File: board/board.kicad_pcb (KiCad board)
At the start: 2 copper layers, 2 parts, among them U1 CC56-12SURKWA

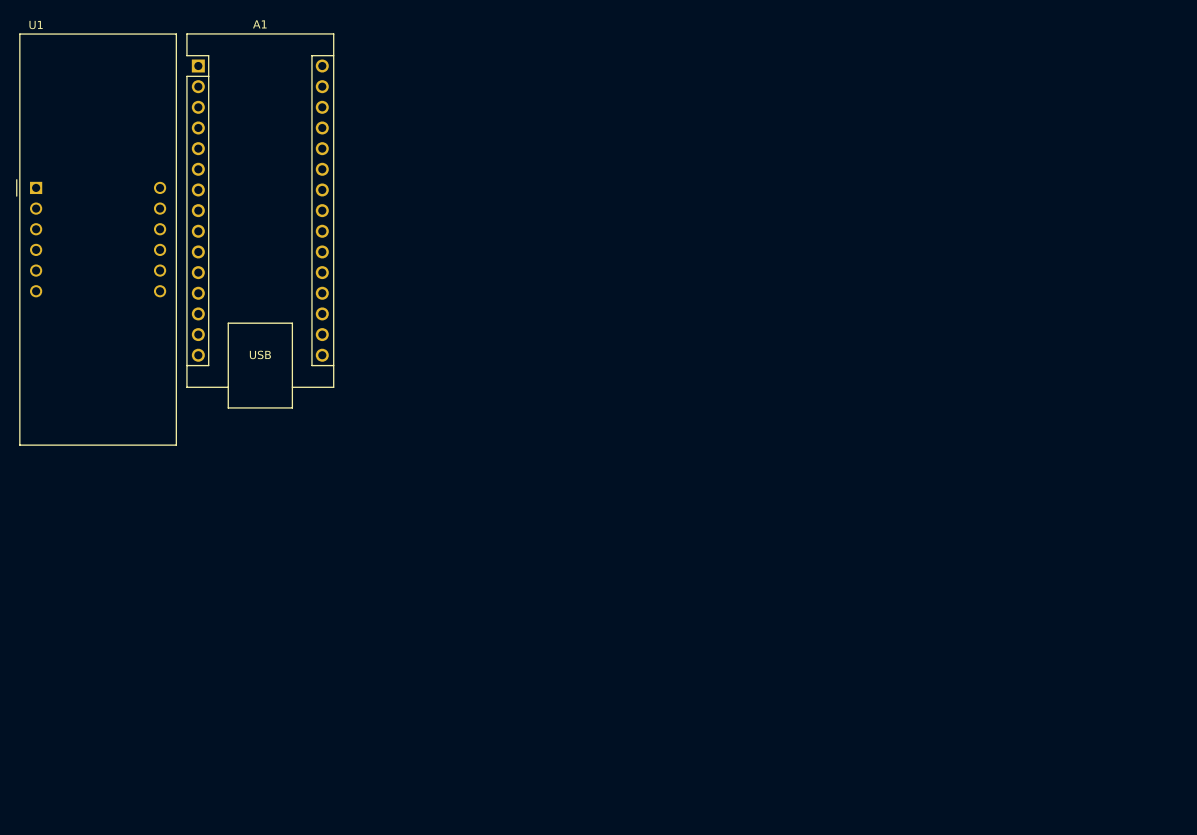
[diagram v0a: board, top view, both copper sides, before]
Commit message: implement part of the wiring
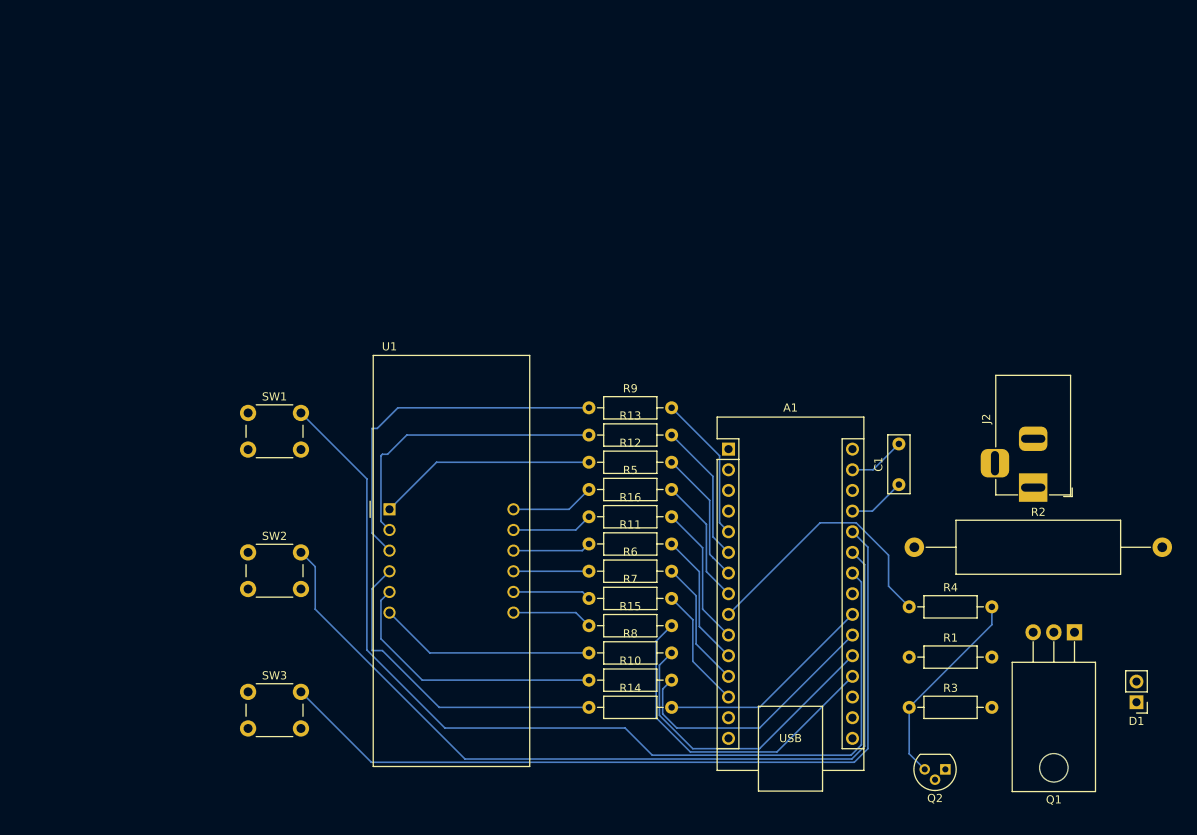
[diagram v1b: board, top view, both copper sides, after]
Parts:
- added C1: 100n, Capacitor_THT:C_Disc_D7.0mm_W2.5mm_P5.00mm, F.Cu at (159.4, 106.0)
- added D1: LED, Connector_PinHeader_2.54mm:PinHeader_1x02_P2.54mm_Vertical, F.Cu at (188.6, 132.7)
- added J2: Barrel_Jack_Switch, Connector_BarrelJack:BarrelJack_Horizontal, F.Cu at (175.9, 106.3)
- added Q1: Q_PMOS_GDS, Package_TO_SOT_THT:TO-220-3_Horizontal_TabDown, F.Cu at (181.0, 124.1)
- added Q2: Q_NPN_ECB, Package_TO_SOT_THT:TO-92, F.Cu at (165.1, 141.0)
- added R1: 10k, Resistor_THT:R_Axial_DIN0207_L6.3mm_D2.5mm_P10.16mm_Horizontal, F.Cu at (160.7, 127.2)
- added R10: 300, Resistor_THT:R_Axial_DIN0207_L6.3mm_D2.5mm_P10.16mm_Horizontal, F.Cu at (121.3, 130.0)
- added R11: 300, Resistor_THT:R_Axial_DIN0207_L6.3mm_D2.5mm_P10.16mm_Horizontal, F.Cu at (121.3, 113.3)
- added R12: 300, Resistor_THT:R_Axial_DIN0207_L6.3mm_D2.5mm_P10.16mm_Horizontal, F.Cu at (121.3, 103.2)
- added R13: 300, Resistor_THT:R_Axial_DIN0207_L6.3mm_D2.5mm_P10.16mm_Horizontal, F.Cu at (121.3, 99.9)
- added R14: 300, Resistor_THT:R_Axial_DIN0207_L6.3mm_D2.5mm_P10.16mm_Horizontal, F.Cu at (121.3, 133.3)
- added R15: 300, Resistor_THT:R_Axial_DIN0207_L6.3mm_D2.5mm_P10.16mm_Horizontal, F.Cu at (121.3, 123.3)
- added R16: 300, Resistor_THT:R_Axial_DIN0207_L6.3mm_D2.5mm_P10.16mm_Horizontal, F.Cu at (121.3, 109.9)
- added R2: 15R, 5W, Resistor_THT:R_Axial_Power_L20.0mm_W6.4mm_P30.48mm, F.Cu at (161.3, 113.7)
- added R3: 10k, Resistor_THT:R_Axial_DIN0207_L6.3mm_D2.5mm_P10.16mm_Horizontal, F.Cu at (160.7, 133.3)
- added R4: 10k, Resistor_THT:R_Axial_DIN0207_L6.3mm_D2.5mm_P10.16mm_Horizontal, F.Cu at (160.7, 121.0)
- added R5: 300, Resistor_THT:R_Axial_DIN0207_L6.3mm_D2.5mm_P10.16mm_Horizontal, F.Cu at (121.3, 106.6)
- added R6: 300, Resistor_THT:R_Axial_DIN0207_L6.3mm_D2.5mm_P10.16mm_Horizontal, F.Cu at (121.3, 116.6)
- added R7: 300, Resistor_THT:R_Axial_DIN0207_L6.3mm_D2.5mm_P10.16mm_Horizontal, F.Cu at (121.3, 120.0)
- added R8: 300, Resistor_THT:R_Axial_DIN0207_L6.3mm_D2.5mm_P10.16mm_Horizontal, F.Cu at (121.3, 126.7)
- added R9: 300, Resistor_THT:R_Axial_DIN0207_L6.3mm_D2.5mm_P10.16mm_Horizontal, F.Cu at (121.3, 96.5)
- added SW1: SW_Push, Button_Switch_THT:SW_PUSH_6mm_H7.3mm, F.Cu at (79.4, 97.2)
- added SW2: SW_Push, Button_Switch_THT:SW_PUSH_6mm_H7.3mm, F.Cu at (79.4, 114.3)
- added SW3: SW_Push, Button_Switch_THT:SW_PUSH_6mm_H7.3mm, F.Cu at (79.4, 131.4)
- moved A1 80.4 mm to (138.4, 101.6)
- moved U1 58.7 mm to (96.8, 109.0)
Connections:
- A1 pad 22: unconnected-(A1-A3-Pad22) -> Net-(A1-A3)
- A1 pad 23: Net-(A1-SDA/A4) -> unconnected-(A1-SDA/A4-Pad23)
- A1 pad 27: unconnected-(A1-+5V-Pad27) -> Net-(A1-+5V)
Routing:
- net Net-(A1-SCL/A5): track 0.00 -> 120.8 mm
- net Net-(A1-A6): track 0.00 -> 108.0 mm
- net Net-(A1-A7): track 0.00 -> 101.4 mm
- net Net-(U1-DPX): track 0.00 -> 43.6 mm
- net Net-(A1-A0): track 0.00 -> 41.8 mm
- net Net-(U1-c): track 0.00 -> 40.2 mm
- net Net-(A1-A1): track 0.00 -> 38.5 mm
- net Net-(U1-d): track 0.00 -> 36.2 mm
- net Net-(U1-g): track 0.00 -> 33.9 mm
- net Net-(A1-A2): track 0.00 -> 33.4 mm
- net Net-(A1-D6): track 0.00 -> 33.4 mm
- net Net-(A1-A3): track 0.00 -> 27.0 mm
- net Net-(U1-e): track 0.00 -> 26.9 mm
- net Net-(U1-CC4): track 0.00 -> 26.6 mm
- net Net-(Q2-B): track 0.00 -> 25.0 mm
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
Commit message: complete the design
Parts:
- added REF**: MountingHole_3.2mm_M3, MountingHole:MountingHole_3.2mm_M3, F.Cu at (190.0, 91.0)
- added REF**: MountingHole_3.2mm_M3, MountingHole:MountingHole_3.2mm_M3, F.Cu at (190.0, 143.0)
- added REF**: MountingHole_3.2mm_M3, MountingHole:MountingHole_3.2mm_M3, F.Cu at (80.0, 91.0)
- added REF**: MountingHole_3.2mm_M3, MountingHole:MountingHole_3.2mm_M3, F.Cu at (80.0, 143.0)
- moved SW1 0.64 mm to (79.4, 96.5)
- moved SW2 0.63 mm to (79.4, 113.7)
- moved SW3 0.63 mm to (79.4, 130.8)
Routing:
- net GND: track 7.02 -> 242.7 mm
- net +9V: track 0.00 -> 73.3 mm
- net Net-(Q1-G): track 0.00 -> 29.4 mm
- net Net-(Q1-D): track 0.00 -> 21.5 mm
- net Net-(D1-A): track 0.00 -> 17.8 mm
- net Net-(A1-A6): track 108.0 -> 115.1 mm
- net Net-(A1-SCL/A5): track 120.8 -> 127.3 mm
- net Net-(A1-A7): track 101.4 -> 107.9 mm
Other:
- board outline added: 118 x 60 mm
- board text added: "+"
- board text added: "-"
- board text added: "<<"
- board text added: "Artificial Sun PCB v1.0 2024.08.11 yasunori.xyz"

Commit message: edit silkscreen
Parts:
- moved REF** 9.50 mm to (89.5, 91.0)
- moved REF** 9.50 mm to (89.5, 143.0)
- moved SW1 8.89 mm to (88.3, 96.5)
- moved SW2 8.89 mm to (88.3, 113.7)
- moved SW3 8.89 mm to (88.3, 130.8)
- moved J2 5.33 mm to (175.9, 101.0)
- moved U1 4.35 mm to (101.1, 109.0)
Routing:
- net Net-(A1-SCL/A5): track 127.3 -> 6.50 mm
- net Net-(A1-A6): track 115.1 -> 6.50 mm
- net GND: track 242.7 -> 140.2 mm
- net Net-(A1-A7): track 107.9 -> 6.50 mm
- net Net-(U1-DPX): track 43.6 -> 0.00 mm
- net Net-(U1-c): track 40.2 -> 0.00 mm
- net Net-(U1-d): track 36.2 -> 0.00 mm
- net Net-(U1-g): track 33.9 -> 0.00 mm
- net Net-(U1-e): track 26.9 -> 0.00 mm
- net Net-(U1-CC4): track 26.6 -> 0.00 mm
- net Net-(U1-CC1): track 10.3 -> 0.00 mm
- net Net-(U1-a): track 9.96 -> 0.00 mm
- net Net-(U1-b): track 9.95 -> 0.00 mm
- net Net-(U1-f): track 9.62 -> 0.00 mm
- net Net-(U1-CC3): track 9.62 -> 0.00 mm
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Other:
- board size 118 x 60 mm -> 108.5 x 60 mm

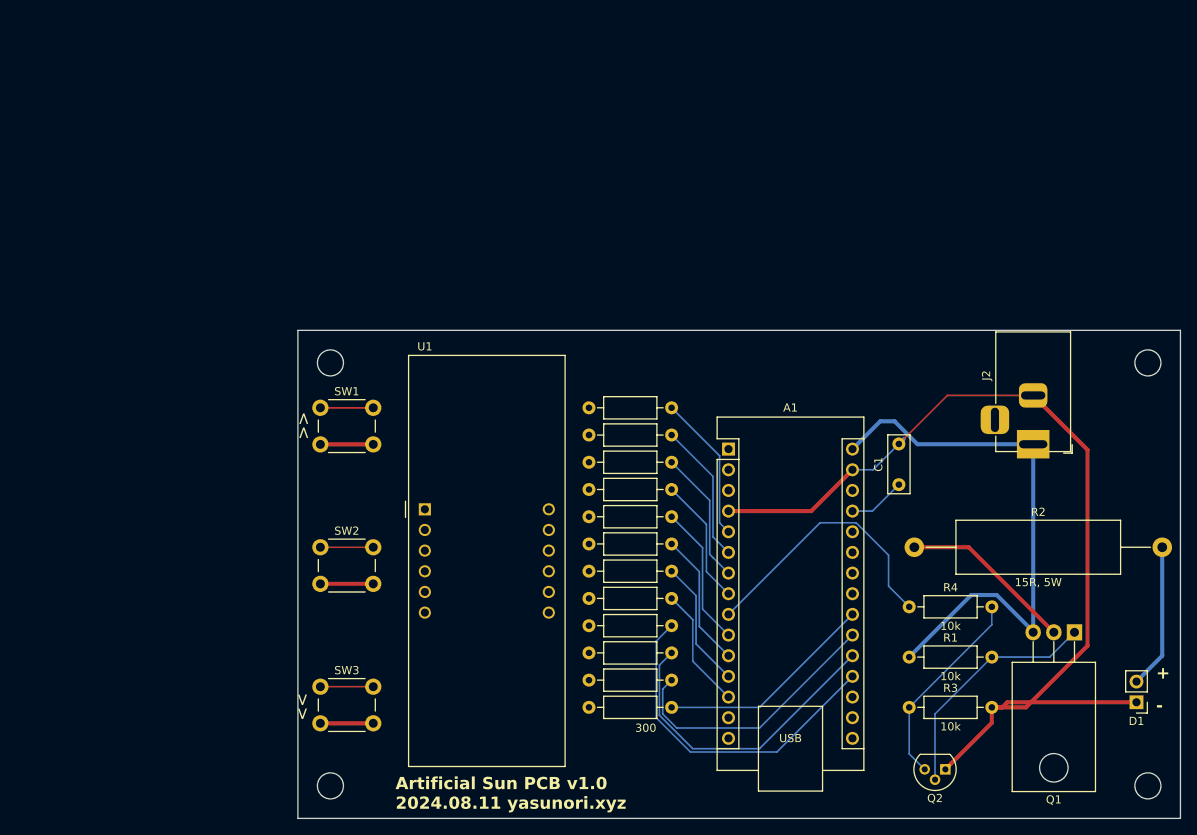
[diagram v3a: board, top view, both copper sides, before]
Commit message: more compact board
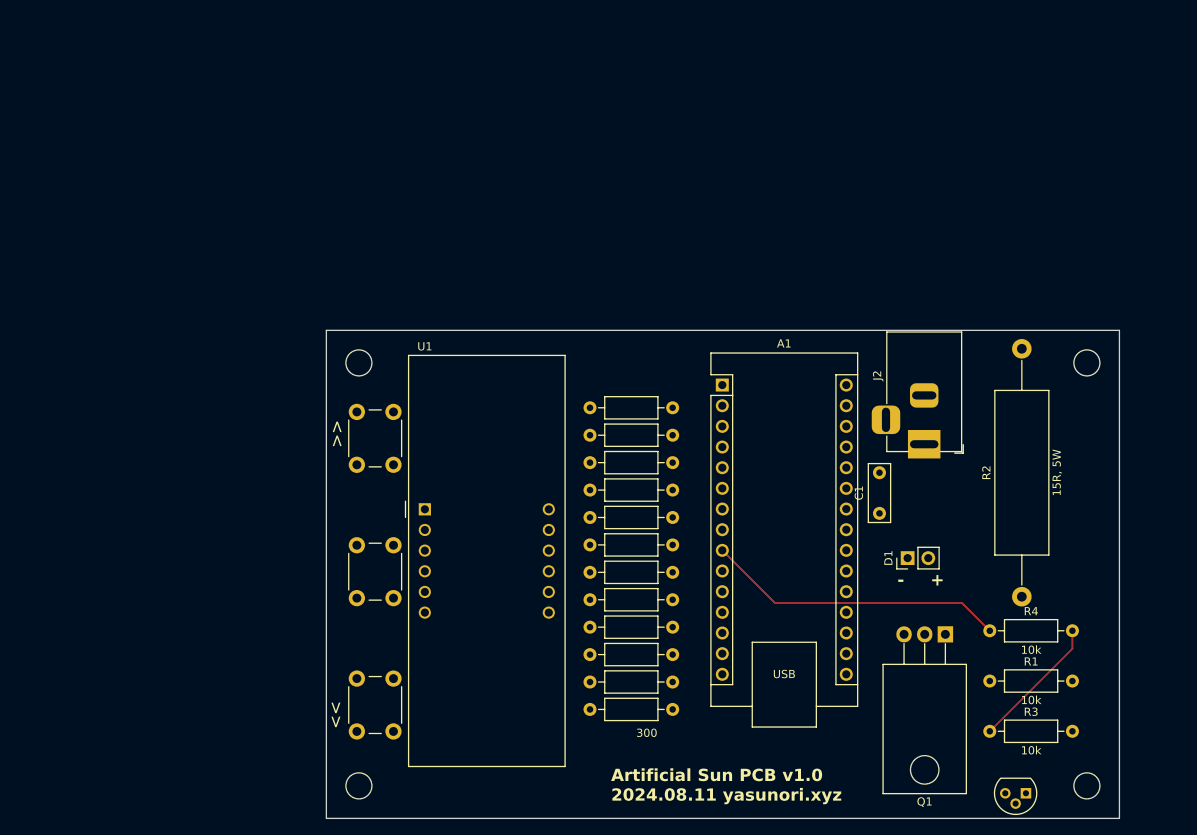
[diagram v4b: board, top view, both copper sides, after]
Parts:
- moved D1 33.3 mm to (160.5, 115.0), turned to 90 degrees
- moved Q1 15.9 mm to (165.1, 124.4)
- moved R2 14.5 mm to (174.5, 119.7), turned to 90 degrees
- moved J2 13.4 mm to (162.5, 101.0)
- moved Q2 10.3 mm to (175.0, 143.9)
- moved R3 10.3 mm to (170.6, 136.3)
- moved R4 10.3 mm to (170.6, 123.9)
- moved R1 10.3 mm to (170.6, 130.1)
- moved SW3 9.04 mm to (97.2, 129.8), turned to -90 degrees
- moved SW1 9.00 mm to (97.2, 97.0), turned to -90 degrees
- moved SW2 8.99 mm to (97.2, 113.4), turned to -90 degrees
- moved A1 7.91 mm to (137.7, 93.7)
- moved REF** 7.50 mm to (182.5, 91.0)
- moved REF** 7.50 mm to (182.5, 143.0)
- moved R8 6.95 mm to (121.4, 133.6)
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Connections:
- R12 pad 2: Net-(A1-D4) -> Net-(A1-D2)
- R9 pad 2: Net-(A1-D2) -> Net-(A1-D4)
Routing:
- net GND: track 140.2 -> 0.00 mm
- net +9V: track 68.3 -> 0.00 mm
- net Net-(A1-A0): track 41.8 -> 0.00 mm
- net Net-(A1-A1): track 38.5 -> 0.00 mm
- net Net-(A1-A2): track 33.4 -> 0.00 mm
- net Net-(Q1-G): track 29.4 -> 0.00 mm
- net Net-(A1-A3): track 27.0 -> 0.00 mm
- net Net-(Q1-D): track 21.5 -> 0.00 mm
- net Net-(A1-D2): track 18.1 -> 0.00 mm
- net Net-(D1-A): track 17.8 -> 0.00 mm
- net Net-(A1-D7): track 17.4 -> 0.00 mm
- net Net-(A1-D3): track 17.3 -> 0.00 mm
- net Net-(A1-D8): track 16.6 -> 0.00 mm
- net Net-(A1-D4): track 16.5 -> 0.00 mm
- net Net-(A1-D9): track 15.8 -> 0.00 mm
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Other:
- board size 108.5 x 60 mm -> 97.5 x 60 mm

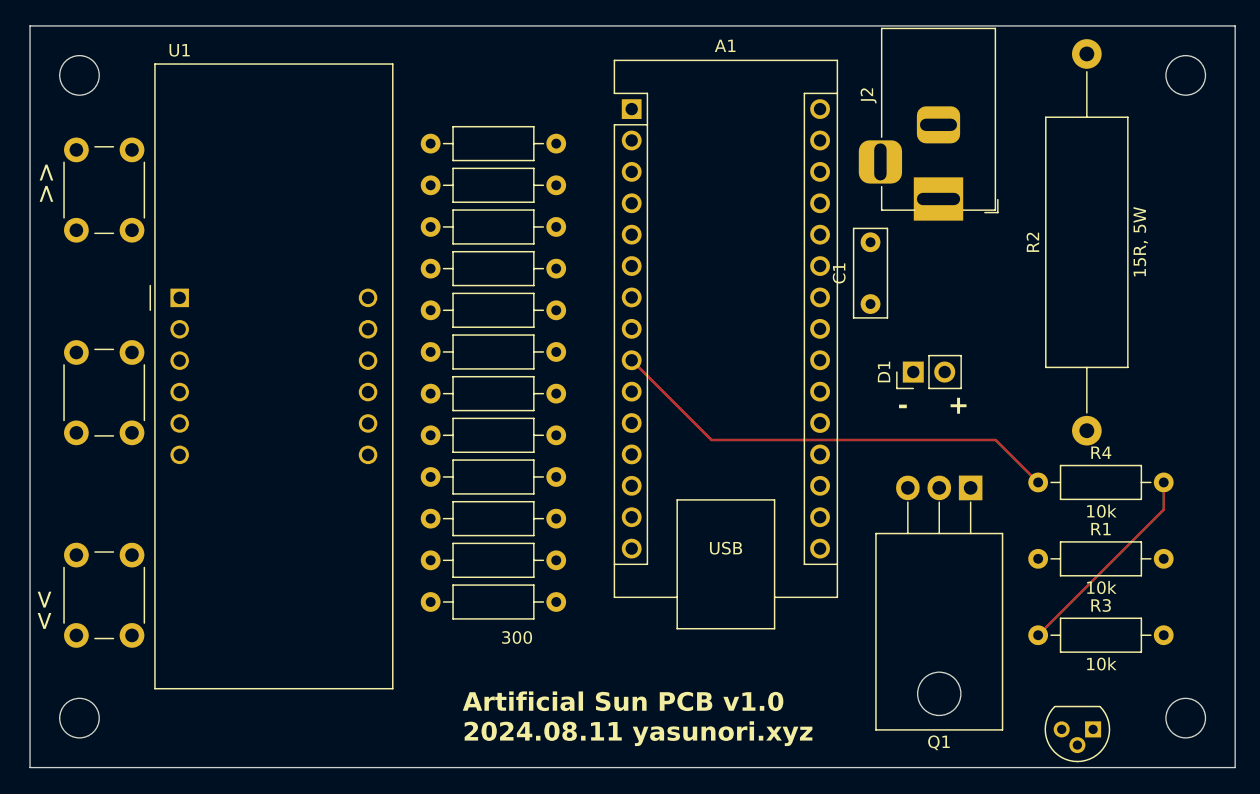
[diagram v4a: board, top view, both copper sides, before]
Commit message: set thick lines for LEDs, probably ready for manufacture
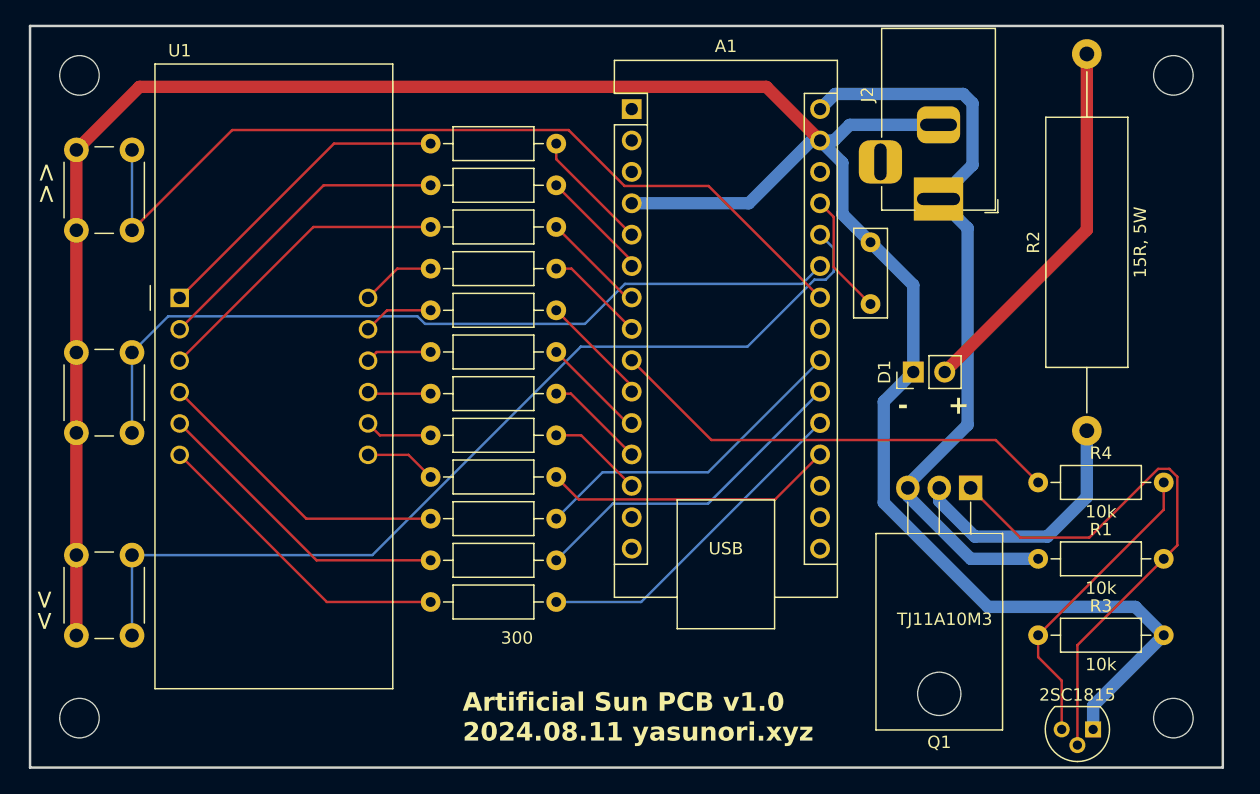
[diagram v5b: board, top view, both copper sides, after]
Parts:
- Q1: value Q_PMOS_GDS -> TJ11A10M3
- Q2: value Q_NPN_ECB -> 2SC1815
- moved REF** 1.00 mm to (181.5, 91.0)
- moved REF** 1.00 mm to (181.5, 143.0)
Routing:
- net GND: track 0.00 -> 201.3 mm
- net Net-(A1-A7): track 0.00 -> 76.2 mm
- net Net-(A1-SCL/A5): track 0.00 -> 71.1 mm
- net Net-(A1-A6): track 0.00 -> 65.6 mm
- net +9V: track 0.00 -> 61.7 mm
- net Net-(Q1-G): track 0.00 -> 46.0 mm
- net Net-(D1-A): track 0.00 -> 30.5 mm
- net Net-(A1-A1): track 0.00 -> 27.3 mm
- net Net-(A1-A2): track 0.00 -> 27.0 mm
- net Net-(A1-A3): track 0.00 -> 26.7 mm
- net Net-(U1-e): track 0.00 -> 25.5 mm
- net Net-(U1-CC4): track 0.00 -> 25.2 mm
- net Net-(U1-d): track 0.00 -> 25.1 mm
- net Net-(U1-g): track 0.00 -> 24.9 mm
- net Net-(U1-DPX): track 0.00 -> 24.8 mm
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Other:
- board size 97.5 x 60 mm -> 96.5 x 60 mm

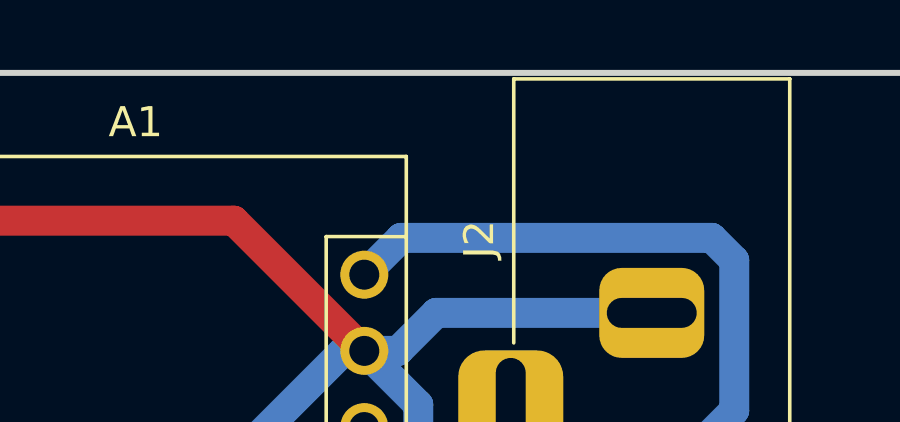
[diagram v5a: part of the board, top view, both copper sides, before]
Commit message: move some symbols on silk screen layer
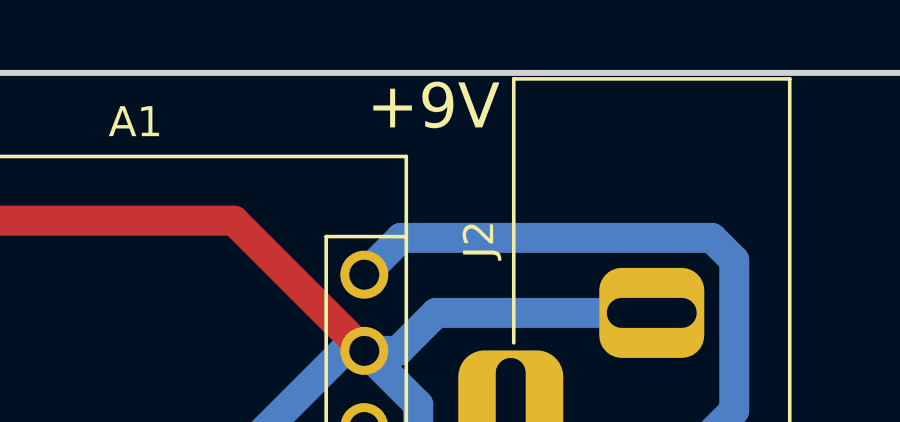
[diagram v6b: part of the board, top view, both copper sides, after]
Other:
- board text added: "+9V"
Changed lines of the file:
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@@
 			(outputformat 1)
 			(mirror no)
-			(drillshape 1)
+			(drillshape 0)
 			(scaleselection 1)
-			(outputdirectory "")
+			(outputdirectory "output/")
 		)
 	)
@@
 			)
 			(justify left bottom)
+		)
+	)
+	(gr_text "+9V"
+		(at 153 89 0)
+		(layer "F.SilkS")
+		(effects
+			(font
+				(size 1.5 1.5)
+				(thickness 0.1)
+			)
+			(justify left bottom)
